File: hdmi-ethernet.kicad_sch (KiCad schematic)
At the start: 121 parts, among them J15 0895-2C1R-GVH, J16 2007435-1, U26 LAN8720A-CP-TR-ABC, U27 KSZ9131RNXC, U28 TPD4E05U06QDQARQ1, U29 TPD4E05U06QDQARQ1, Y3 ABM8G-25.000MHZ-18-D2Y-T, Y4 ABM8G-25.000MHZ-18-D2Y-T

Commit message: Loclib
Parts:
- C252, C256, C258, C263: footprint antmicro-footprints:0402-cap -> K410T-devboard-footprints:0402-cap; symbol antmicroCapacitors0402:C_22p_0402 -> K410T-devboard:C_22p_0402
- C253, C254, C255, C271, C274, C280, C285, C292, C293: footprint antmicro-footprints:0402-cap -> K410T-devboard-footprints:0402-cap; symbol antmicroCapacitors0402:C_10u_0402 -> K410T-devboard:C_10u_0402
- C257, C259, C260, C261, C262, C264, C265, C267, C268, C269, C270, C272, C277, C281, C282, C283, C284, C286, C287, C288, C289, C290, C291, C398: footprint antmicro-footprints:0402-cap_EIA -> K410T-devboard-footprints:0402-cap_EIA; symbol antmicroCapacitors0402:C_100n_0402_EIA -> K410T-devboard:C_100n_0402_EIA
- C273, C275, C276, C279: footprint antmicro-footprints:0402-cap -> K410T-devboard-footprints:0402-cap; symbol antmicroCapacitors0402:C_10p_0402 -> K410T-devboard:C_10p_0402
- C278: footprint antmicro-footprints:0402-cap -> K410T-devboard-footprints:0402-cap; symbol antmicroCapacitors0402:C_10n_0402 -> K410T-devboard:C_10n_0402
- D31: footprint antmicro-footprints:SOD-523 -> K410T-devboard-footprints:SOD-523; symbol antmicroDiodesRectifiersSingle:RB521S30T1G -> K410T-devboard:RB521S30T1G
- FB10, FB7, FB8, FB9: footprint antmicro-footprints:0603-res -> K410T-devboard-footprints:0603-res; symbol antmicroFerriteBeadsandChips:BLM18PG121SN1D -> K410T-devboard:BLM18PG121SN1D
- J15: footprint antmicro-footprints:0895-2C1R-GVH -> K410T-devboard-footprints:0895-2C1R-GVH; symbol antmicroModularConnectorsJacksWithMagnetics:0895-2C1R-GVH -> K410T-devboard:0895-2C1R-GVH
- J16: footprint antmicro-footprints:TE_2007435-1 -> K410T-devboard-footprints:TE_2007435-1; symbol antmicroUSBDVIHDMIConnectors:2007435-1 -> K410T-devboard:2007435-1
- R197, R199, R200, R201, R202, R203, R204, R205, R206, R207, R208, R219, R220, R221, R222, R223, R224, R239: footprint antmicro-footprints:0402-res -> K410T-devboard-footprints:0402-res; symbol antmicroResistors0402:R_10k_0402 -> K410T-devboard:R_10k_0402
- R198, R240: footprint antmicro-footprints:0402-res -> K410T-devboard-footprints:0402-res; symbol antmicroResistors0402:R_1k_0402 -> K410T-devboard:R_1k_0402
- R209, R210, R211, R212, R213, R214, R215, R216, R217, R218, R225, R226, R227, R228, R229, R230: footprint antmicro-footprints:0402-res -> K410T-devboard-footprints:0402-res; symbol antmicroResistors0402:R_2k2_0402 -> K410T-devboard:R_2k2_0402
- R231, R232, R233, R234, R235, R236, R237, R238: footprint antmicro-footprints:0402-res -> K410T-devboard-footprints:0402-res; symbol antmicroResistors0402:R_10R_1%_0402 -> K410T-devboard:R_10R_1%_0402
- R241, R242: footprint antmicro-footprints:0402-res -> K410T-devboard-footprints:0402-res; symbol antmicroResistors0402:R_1M0_0402 -> K410T-devboard:R_1M0_0402
- R243, R254, R255, R256, R257, R258, R259, R260, R261: footprint antmicro-footprints:0402-res -> K410T-devboard-footprints:0402-res; symbol antmicroResistors0402:R_0R_0402 -> K410T-devboard:R_0R_0402
- R244, R248: footprint antmicro-footprints:0402-res -> K410T-devboard-footprints:0402-res; symbol antmicroResistors0402:R_12k_0402 -> K410T-devboard:R_12k_0402
- R245, R247, R249, R250: footprint antmicro-footprints:0402-res -> K410T-devboard-footprints:0402-res; symbol antmicroResistors0402:R_49R9_0402 -> K410T-devboard:R_49R9_0402
- R246: footprint antmicro-footprints:0603-res -> K410T-devboard-footprints:0603-res; symbol antmicroResistors0603:R_10R_0603 -> K410T-devboard:R_10R_0603
- R251, R252, R262, R263: footprint antmicro-footprints:0603-res -> K410T-devboard-footprints:0603-res; symbol antmicroResistors0603:R_220R_0603 -> K410T-devboard:R_220R_0603
- U26: footprint antmicro-footprints:QFN-24-1EP_4x4mm_P0.5mm_EP2.6x2.6mm -> K410T-devboard-footprints:QFN-24-1EP_4x4mm_P0.5mm_EP2.6x2.6mm; symbol antmicroInterfaceControllers:LAN8720A-CP-TR-ABC -> K410T-devboard:LAN8720A-CP-TR-ABC
- U27: footprint antmicro-footprints:QFN-48-Microchip-QFN77-48LD-PL-2 -> K410T-devboard-footprints:QFN-48-Microchip-QFN77-48LD-PL-2; symbol antmicroInterfaceControllers:KSZ9131RNXC -> K410T-devboard:KSZ9131RNXC
- U28, U29: footprint antmicro-footprints:USON-10_2.5x1.0mm_P0.5mm -> K410T-devboard-footprints:USON-10_2.5x1.0mm_P0.5mm; symbol antmicroTVSDiodes:TPD4E05U06QDQARQ1 -> K410T-devboard:TPD4E05U06QDQARQ1
- Y3, Y4: footprint antmicro-footprints:KX-7 -> K410T-devboard-footprints:KX-7; symbol antmicroCrystals:ABM8G-25.000MHZ-18-D2Y-T -> K410T-devboard:ABM8G-25.000MHZ-18-D2Y-T

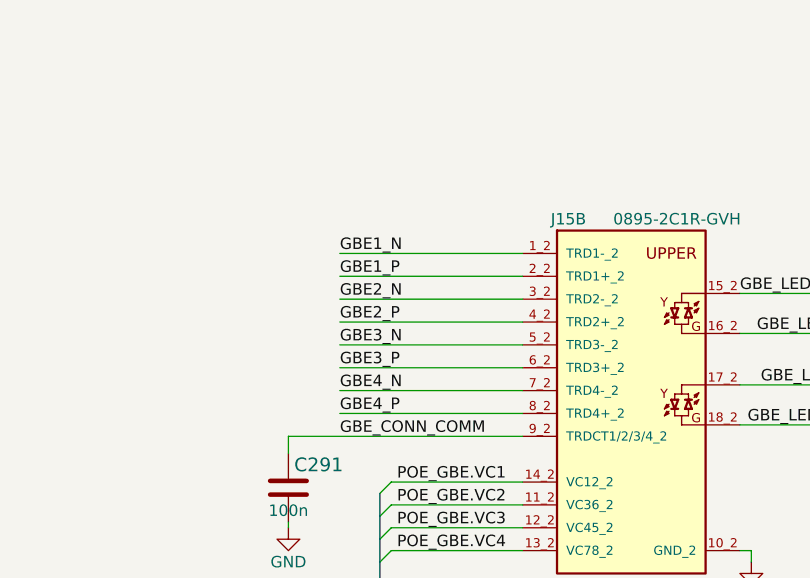
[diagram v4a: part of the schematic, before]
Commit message: Swap GBE pairs for easier routing
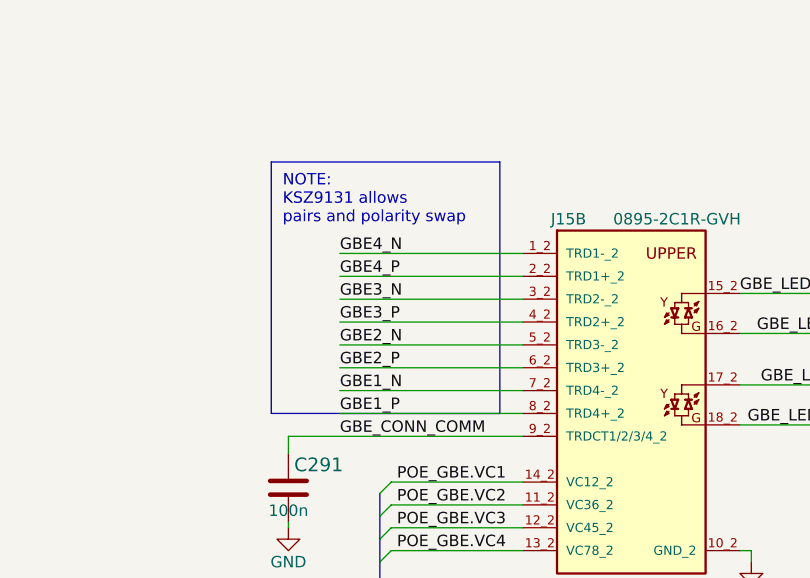
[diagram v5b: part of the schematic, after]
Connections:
- net GBE1_N: now also J15.7_2 (TRD4-_2); no longer J15.1_2 (TRD1-_2)
- net GBE1_P: now also J15.8_2 (TRD4+_2); no longer J15.2_2 (TRD1+_2)
- net GBE2_N: now also J15.5_2 (TRD3-_2); no longer J15.3_2 (TRD2-_2)
- net GBE2_P: now also J15.6_2 (TRD3+_2); no longer J15.4_2 (TRD2+_2)
- net GBE3_N: now also J15.3_2 (TRD2-_2); no longer J15.5_2 (TRD3-_2)
- net GBE3_P: now also J15.4_2 (TRD2+_2); no longer J15.6_2 (TRD3+_2)
- net GBE4_N: now also J15.1_2 (TRD1-_2); no longer J15.7_2 (TRD4-_2)
- net GBE4_P: now also J15.2_2 (TRD1+_2); no longer J15.8_2 (TRD4+_2)
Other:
- note added: "NOTE: KSZ9131 allows pairs and polarity swap"
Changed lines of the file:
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@@
     (stroke (width 0) (type default) (color 0 0 0 0))
   )
+  (polyline (pts (xy 325.755 84.455) (xy 351.155 84.455))
+    (stroke (width 0) (type default) (color 0 0 0 0))
+  )
   (wire (pts (xy 51.435 254) (xy 25.4 254))
     (stroke (width 0) (type default) (color 0 0 0 0))
@@
     (stroke (width 0) (type default) (color 0 0 0 0))
   )
+  (polyline (pts (xy 351.155 112.395) (xy 351.155 84.455))
+    (stroke (width 0) (type default) (color 0 0 0 0))
+  )
   (wire (pts (xy 324.485 213.36) (xy 324.485 214.63))
     (stroke (width 0) (type default) (color 0 0 0 0))
@@
     (stroke (width 0) (type default) (color 0 0 0 0))
   )
+  (polyline (pts (xy 325.755 112.395) (xy 351.155 112.395))
+    (stroke (width 0) (type default) (color 0 0 0 0))
+  )
   (wire (pts (xy 347.98 168.91) (xy 378.46 168.91))
     (stroke (width 0) (type default) (color 0 0 0 0))
@@
     (stroke (width 0) (type solid) (color 0 0 0 0))
   )
+  (polyline (pts (xy 325.755 84.455) (xy 325.755 112.395))
+    (stroke (width 0) (type default) (color 0 0 0 0))
+  )
   (wire (pts (xy 379.095 128.905) (xy 379.095 127.635))
     (stroke (width 0) (type default) (color 0 0 0 0))
@@
     (effects (font (size 1.27 1.27)) (justify left bottom))
   )
+  (text "NOTE:\nKSZ9131 allows \npairs and polarity swap" (at 327.025 91.44 0)
+    (effects (font (size 1.27 1.27)) (justify left bottom))
+  )
   (text "~{INTSEL}" (at 68.58 245.11 0)
     (effects (font (size 1.27 1.27)) (justify left bottom))
@@
     (effects (font (size 1.27 1.27)) (justify left bottom))
   )
-  (label "GBE2_P" (at 333.375 102.235 0)
+  (label "GBE2_P" (at 333.375 107.315 0)
     (effects (font (size 1.27 1.27)) (justify left bottom))
   )
@@
     (effects (font (size 1.27 1.27)) (justify left bottom))
   )
-  (label "GBE1_P" (at 333.375 97.155 0)
+  (label "GBE1_P" (at 333.375 112.395 0)
     (effects (font (size 1.27 1.27)) (justify left bottom))
   )
@@
     (effects (font (size 1.27 1.27)) (justify right bottom))
   )
-  (label "GBE4_N" (at 333.375 109.855 0)
+  (label "GBE4_N" (at 333.375 94.615 0)
     (effects (font (size 1.27 1.27)) (justify left bottom))
   )
@@
     (effects (font (size 1.27 1.27)) (justify left bottom))
   )
-  (label "GBE1_N" (at 333.375 94.615 0)
+  (label "GBE1_N" (at 333.375 109.855 0)
     (effects (font (size 1.27 1.27)) (justify left bottom))
   )
-  (label "GBE3_P" (at 333.375 107.315 0)
+  (label "GBE3_P" (at 333.375 102.235 0)
     (effects (font (size 1.27 1.27)) (justify left bottom))
   )
@@
     (effects (font (size 1.27 1.27)) (justify right bottom))
   )
-  (label "GBE4_P" (at 333.375 112.395 0)
+  (label "GBE4_P" (at 333.375 97.155 0)
     (effects (font (size 1.27 1.27)) (justify left bottom))
   )
@@
     (effects (font (size 1.27 1.27)) (justify left bottom))
   )
-  (label "GBE2_N" (at 333.375 99.695 0)
+  (label "GBE2_N" (at 333.375 104.775 0)
     (effects (font (size 1.27 1.27)) (justify left bottom))
   )
@@
     (effects (font (size 1.27 1.27)) (justify left bottom))
   )
-  (label "GBE3_N" (at 333.375 104.775 0)
+  (label "GBE3_N" (at 333.375 99.695 0)
     (effects (font (size 1.27 1.27)) (justify left bottom))
   )

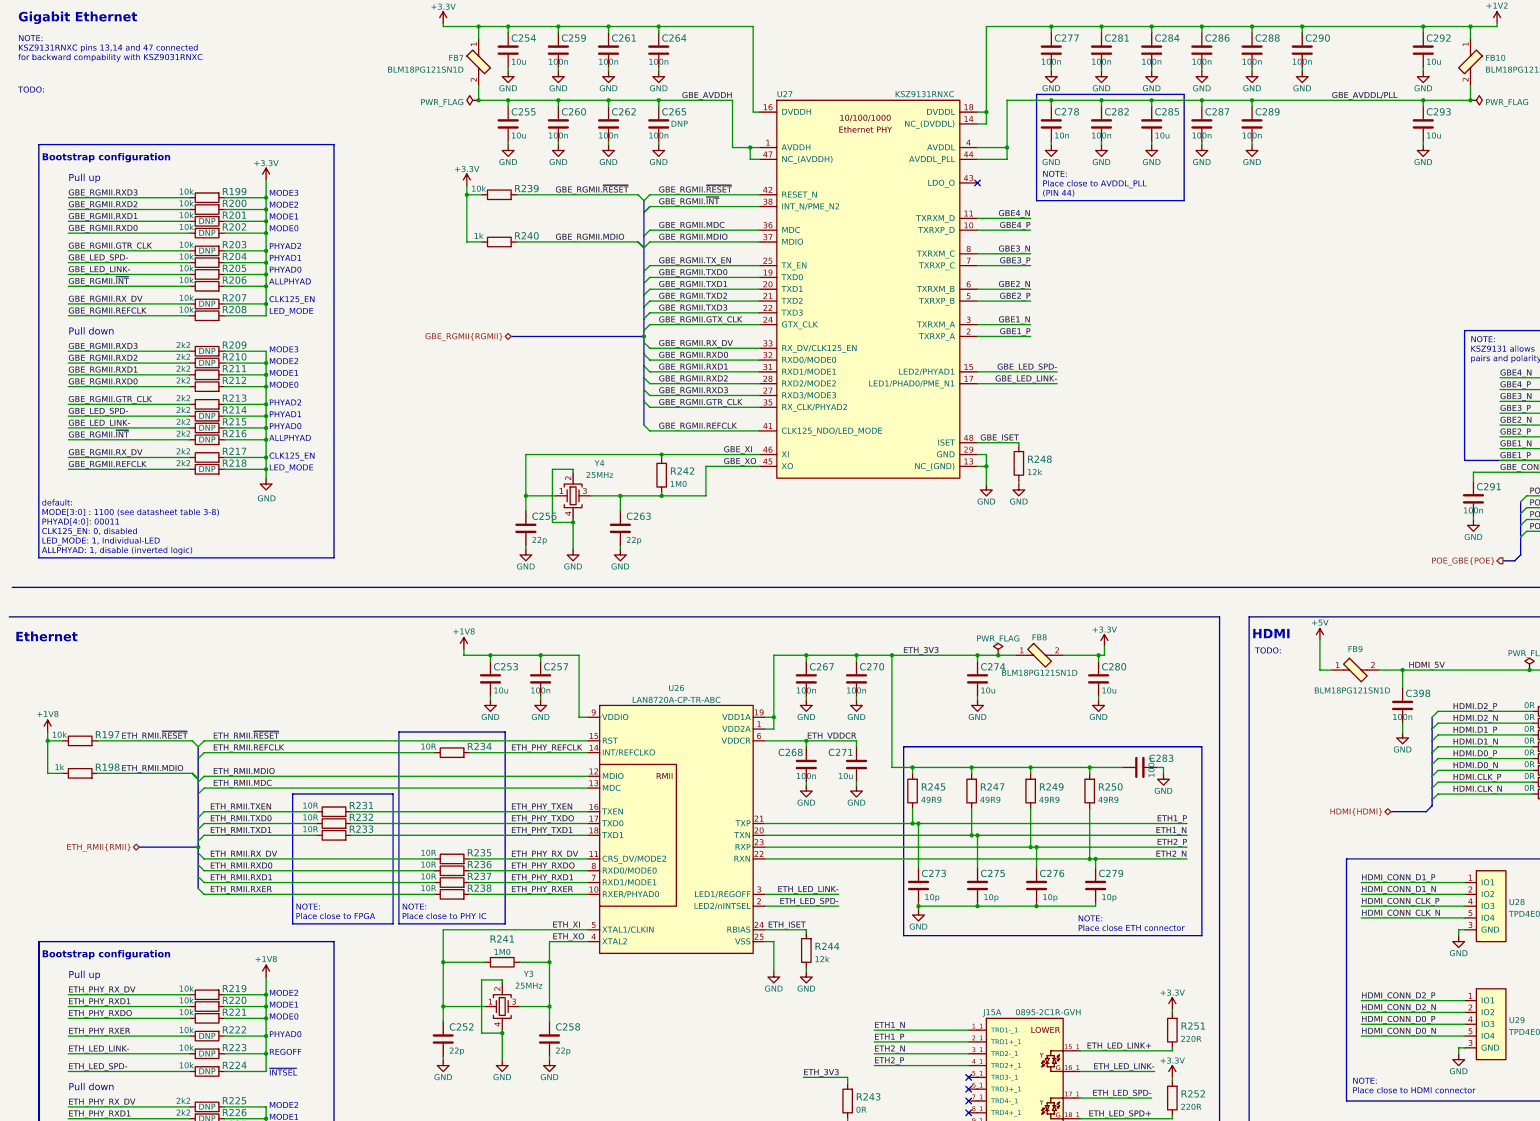
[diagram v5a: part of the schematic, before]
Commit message: Remove TODO, update HDMI ESD connections based on routing
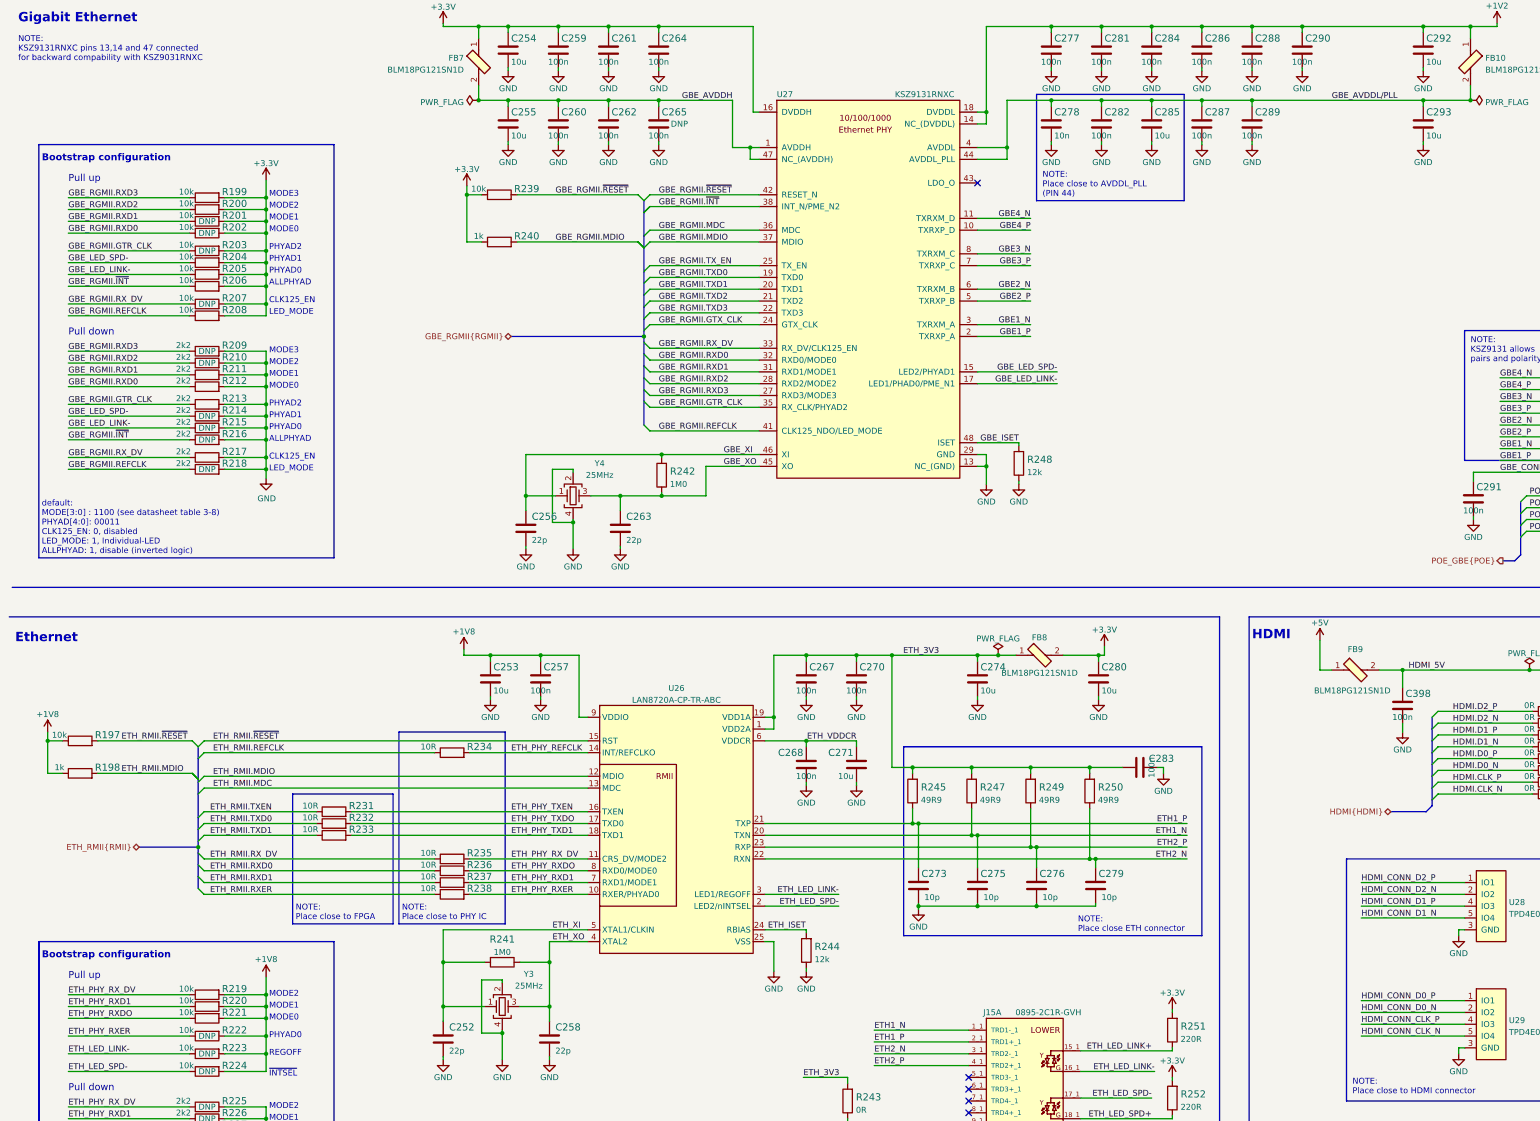
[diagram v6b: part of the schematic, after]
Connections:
- net HDMI_CONN_CLK_N: now also U29.5 (IO4), U29.6 (IO4); no longer U28.5 (IO4), U28.6 (IO4)
- net HDMI_CONN_CLK_P: now also U29.4 (IO3), U29.7 (IO3); no longer U28.4 (IO3), U28.7 (IO3)
- net HDMI_CONN_D0_N: now also U29.2 (IO2), U29.9 (IO2); no longer U29.5 (IO4), U29.6 (IO4)
- net HDMI_CONN_D0_P: now also U29.1 (IO1), U29.10 (IO1); no longer U29.4 (IO3), U29.7 (IO3)
- net HDMI_CONN_D1_N: now also U28.5 (IO4), U28.6 (IO4); no longer U28.2 (IO2), U28.9 (IO2)
- net HDMI_CONN_D1_P: now also U28.4 (IO3), U28.7 (IO3); no longer U28.1 (IO1), U28.10 (IO1)
- net HDMI_CONN_D2_N: now also U28.2 (IO2), U28.9 (IO2); no longer U29.2 (IO2), U29.9 (IO2)
- net HDMI_CONN_D2_P: now also U28.1 (IO1), U28.10 (IO1); no longer U29.1 (IO1), U29.10 (IO1)
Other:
- note removed: "TODO:"
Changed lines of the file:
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@@
-    (effects (font (size 1.27 1.27)) (justify left bottom))
-  )
-  (text "TODO:" (at 14.605 33.655 0)
     (effects (font (size 1.27 1.27)) (justify left bottom))
   )
@@
     (effects (font (size 1.27 1.27)) (justify left bottom))
   )
-  (text "TODO:\n" (at 280.67 154.305 0)
-    (effects (font (size 1.27 1.27)) (justify left bottom))
-  )
   (text "NOTE:\nPlace close to HDMI connector" (at 301.625 248.92 0)
     (effects (font (size 1.27 1.27)) (justify left bottom))
@@
     (effects (font (size 1.27 1.27)) (justify left bottom))
   )
-  (label "HDMI_CONN_CLK_N" (at 303.53 210.82 0)
+  (label "HDMI_CONN_CLK_N" (at 303.53 236.22 0)
     (effects (font (size 1.27 1.27)) (justify left bottom))
   )
@@
     (effects (font (size 1.27 1.27)) (justify left bottom))
   )
-  (label "HDMI_CONN_D1_P" (at 303.53 203.2 0)
+  (label "HDMI_CONN_D1_P" (at 303.53 208.28 0)
     (effects (font (size 1.27 1.27)) (justify left bottom))
   )
@@
     (effects (font (size 1.27 1.27)) (justify left bottom))
   )
-  (label "HDMI_CONN_D2_N" (at 303.53 231.14 0)
+  (label "HDMI_CONN_D2_N" (at 303.53 205.74 0)
     (effects (font (size 1.27 1.27)) (justify left bottom))
   )
@@
     (effects (font (size 1.27 1.27)) (justify left bottom))
   )
-  (label "HDMI_CONN_CLK_P" (at 303.53 208.28 0)
+  (label "HDMI_CONN_CLK_P" (at 303.53 233.68 0)
     (effects (font (size 1.27 1.27)) (justify left bottom))
   )
@@
     (effects (font (size 1.27 1.27)) (justify right bottom))
   )
-  (label "HDMI_CONN_D0_N" (at 303.53 236.22 0)
-    (effects (font (size 1.27 1.27)) (justify left bottom))
-  )
-  (label "HDMI_CONN_D2_P" (at 303.53 228.6 0)
+  (label "HDMI_CONN_D0_N" (at 303.53 231.14 0)
+    (effects (font (size 1.27 1.27)) (justify left bottom))
+  )
+  (label "HDMI_CONN_D2_P" (at 303.53 203.2 0)
     (effects (font (size 1.27 1.27)) (justify left bottom))
   )
@@
     (effects (font (size 1.27 1.27)) (justify right bottom))
   )
-  (label "HDMI_CONN_D0_P" (at 303.53 233.68 0)
+  (label "HDMI_CONN_D0_P" (at 303.53 228.6 0)
     (effects (font (size 1.27 1.27)) (justify left bottom))
   )
@@
     (effects (font (size 1.27 1.27)) (justify left bottom))
   )
-  (label "HDMI_CONN_D1_N" (at 303.53 205.74 0)
-    (effects (font (size 1.27 1.27)) (justify left bottom))
-  )
+  (label "HDMI_CONN_D1_N" (at 303.53 210.82 0)
+    (effects (font (size 1.27 1.27)) (justify left bottom))
+  )
